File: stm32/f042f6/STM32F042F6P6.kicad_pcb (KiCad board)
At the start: 2 copper layers, 22.9 x 32.1 mm, 29 parts, among them J1 USB_C_REC_16PIN, J2 STLINK, J3 L, J4 R, SW1 BOOT0, U1 XC6220B331MR, U2 STM32F042F6Px, Y1 8 MHz

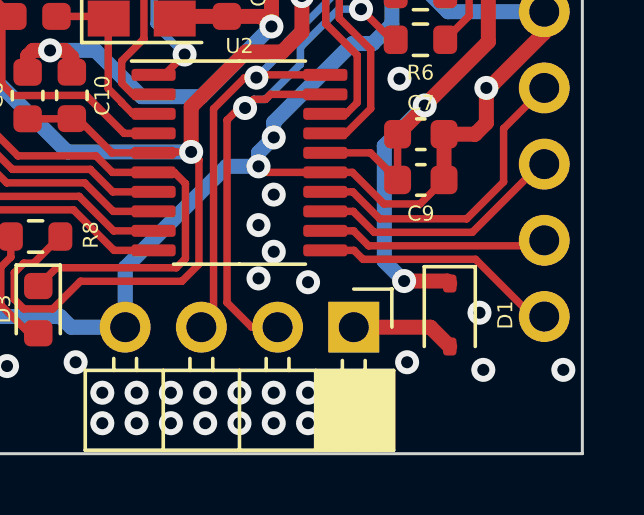
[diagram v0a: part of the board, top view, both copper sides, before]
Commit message: WIP: F070F6P6, Fix: Diode direction corrected for F042F6P6.
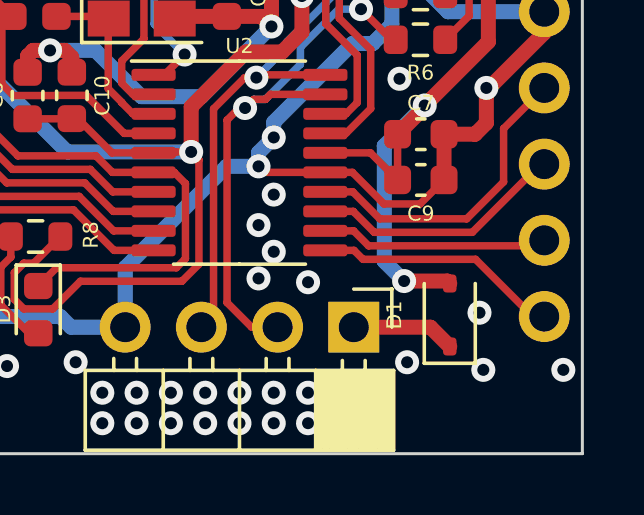
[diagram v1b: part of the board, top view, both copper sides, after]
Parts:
- C3, C4: value 8pF -> 32pF
- turned D1 to 90 degrees
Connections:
- D1 pad 1: +3.3V -> Net-(D1-K)
- D1 pad 2: Net-(D1-A) -> +3.3V
- J2 pad 1: Net-(D1-A) -> Net-(D1-K)
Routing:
- net Net-(D1-K): track 0.00 -> 3.47 mm
- net Net-(D1-A): track 3.47 -> 0.00 mm
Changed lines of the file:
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@@
   (net 6 "+3.3V")
   (net 7 "NRST")
-  (net 8 "Net-(D1-A)")
+  (net 8 "Net-(D1-K)")
   (net 9 "Net-(D2-A)")
   (net 10 "Net-(J1-CC1)")
@@
       (stroke (width 0.1) (type solid)) (layer "F.Fab"))
     (pad "1" thru_hole rect (at 0 0 270) (size 1.7 1.7) (drill 1) (layers "*.Cu" "*.Mask")
-      (net 8 "Net-(D1-A)") (pinfunction "Pin_1") (pintype "passive"))
+      (net 8 "Net-(D1-K)") (pinfunction "Pin_1") (pintype "passive"))
     (pad "2" thru_hole oval (at 0 2.54 270) (size 1.7 1.7) (drill 1) (layers "*.Cu" "*.Mask")
       (net 16 "SWDIO") (pinfunction "Pin_2") (pintype "passive"))
@@
         (effects (font (size 0.5 0.5) (thickness 0.125)))
     )
-    (fp_text value "8pF" (at 0 1.43 90) (layer "F.Fab")
+    (fp_text value "32pF" (at 0 1.43 90) (layer "F.Fab")
         (effects (font (size 1 1) (thickness 0.15)))
     )
@@
   )
   (footprint "Diode_SMD:D_SOD-323" (layer "F.Cu")
-    (at 97.1804 104.0892 -90)
+    (at 97.1804 104.0892 90)
     (descr "SOD-323")
     (tags "SOD-323")
@@
     (fp_line (start 0.9 0.7) (end -0.9 0.7)
       (stroke (width 0.1) (type solid)) (layer "F.Fab"))
-    (pad "1" smd roundrect (at -1.05 0 270) (size 0.6 0.45) (layers "F.Cu" "F.Paste" "F.Mask") (roundrect_rratio 0.25)
-      (net 6 "+3.3V") (pinfunction "K") (pintype "passive"))
-    (pad "2" smd roundrect (at 1.05 0 270) (size 0.6 0.45) (layers "F.Cu" "F.Paste" "F.Mask") (roundrect_rratio 0.25)
-      (net 8 "Net-(D1-A)") (pinfunction "A") (pintype "passive"))
+    (pad "1" smd roundrect (at -1.05 0 90) (size 0.6 0.45) (layers "F.Cu" "F.Paste" "F.Mask") (roundrect_rratio 0.25)
+      (net 8 "Net-(D1-K)") (pinfunction "K") (pintype "passive"))
+    (pad "2" smd roundrect (at 1.05 0 90) (size 0.6 0.45) (layers "F.Cu" "F.Paste" "F.Mask") (roundrect_rratio 0.25)
+      (net 6 "+3.3V") (pinfunction "A") (pintype "passive"))
     (model "${KICAD6_3DMODEL_DIR}/Diode_SMD.3dshapes/D_SOD-323.wrl"
       (offset (xyz 0 0 0))
@@
         (effects (font (size 0.5 0.5) (thickness 0.125)))
     )
-    (fp_text value "8pF" (at 0 1.43 90) (layer "F.Fab")
-        (effects (font (size 1 1) (thickness 0.15)))
-    )
+    (fp_text value "32pF" (at 0 1.43 90) (layer "F.Fab")
+        (effects (font (size 1 1) (thickness 0.15)))
+    )

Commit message: Fix: Diode direction corrected.
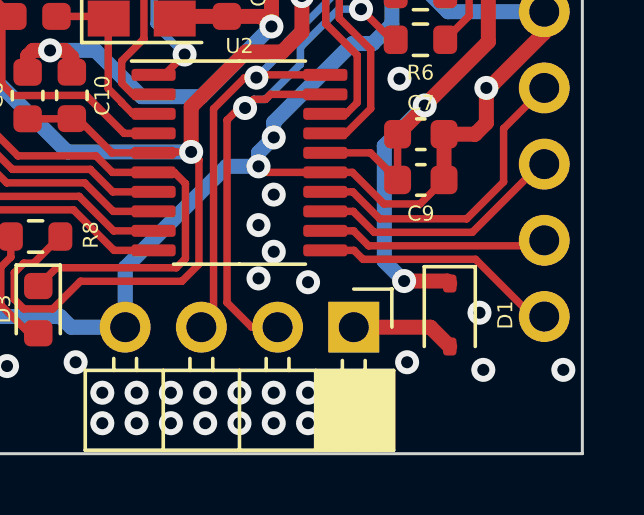
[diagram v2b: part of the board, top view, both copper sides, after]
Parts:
- turned D1 to -90 degrees
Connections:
- D1 pad 1: Net-(D1-K) -> +3.3V
- D1 pad 2: +3.3V -> Net-(D1-A)
- J2 pad 1: Net-(D1-K) -> Net-(D1-A)
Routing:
- net Net-(D1-K): track 3.47 -> 0.00 mm
- net Net-(D1-A): track 0.00 -> 3.47 mm
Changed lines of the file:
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@@
   (net 6 "+3.3V")
   (net 7 "NRST")
-  (net 8 "Net-(D1-K)")
+  (net 8 "Net-(D1-A)")
   (net 9 "Net-(D2-A)")
   (net 10 "Net-(J1-CC1)")
@@
       (stroke (width 0.1) (type solid)) (layer "F.Fab"))
     (pad "1" thru_hole rect (at 0 0 270) (size 1.7 1.7) (drill 1) (layers "*.Cu" "*.Mask")
-      (net 8 "Net-(D1-K)") (pinfunction "Pin_1") (pintype "passive"))
+      (net 8 "Net-(D1-A)") (pinfunction "Pin_1") (pintype "passive"))
     (pad "2" thru_hole oval (at 0 2.54 270) (size 1.7 1.7) (drill 1) (layers "*.Cu" "*.Mask")
       (net 16 "SWDIO") (pinfunction "Pin_2") (pintype "passive"))
@@
   )
   (footprint "Diode_SMD:D_SOD-323" (layer "F.Cu")
-    (at 97.1804 104.0892 90)
+    (at 97.1804 104.0892 -90)
     (descr "SOD-323")
     (tags "SOD-323")
@@
     (fp_line (start 0.9 0.7) (end -0.9 0.7)
       (stroke (width 0.1) (type solid)) (layer "F.Fab"))
-    (pad "1" smd roundrect (at -1.05 0 90) (size 0.6 0.45) (layers "F.Cu" "F.Paste" "F.Mask") (roundrect_rratio 0.25)
-      (net 8 "Net-(D1-K)") (pinfunction "K") (pintype "passive"))
-    (pad "2" smd roundrect (at 1.05 0 90) (size 0.6 0.45) (layers "F.Cu" "F.Paste" "F.Mask") (roundrect_rratio 0.25)
-      (net 6 "+3.3V") (pinfunction "A") (pintype "passive"))
+    (pad "1" smd roundrect (at -1.05 0 270) (size 0.6 0.45) (layers "F.Cu" "F.Paste" "F.Mask") (roundrect_rratio 0.25)
+      (net 6 "+3.3V") (pinfunction "K") (pintype "passive"))
+    (pad "2" smd roundrect (at 1.05 0 270) (size 0.6 0.45) (layers "F.Cu" "F.Paste" "F.Mask") (roundrect_rratio 0.25)
+      (net 8 "Net-(D1-A)") (pinfunction "A") (pintype "passive"))
     (model "${KICAD6_3DMODEL_DIR}/Diode_SMD.3dshapes/D_SOD-323.wrl"
       (offset (xyz 0 0 0))

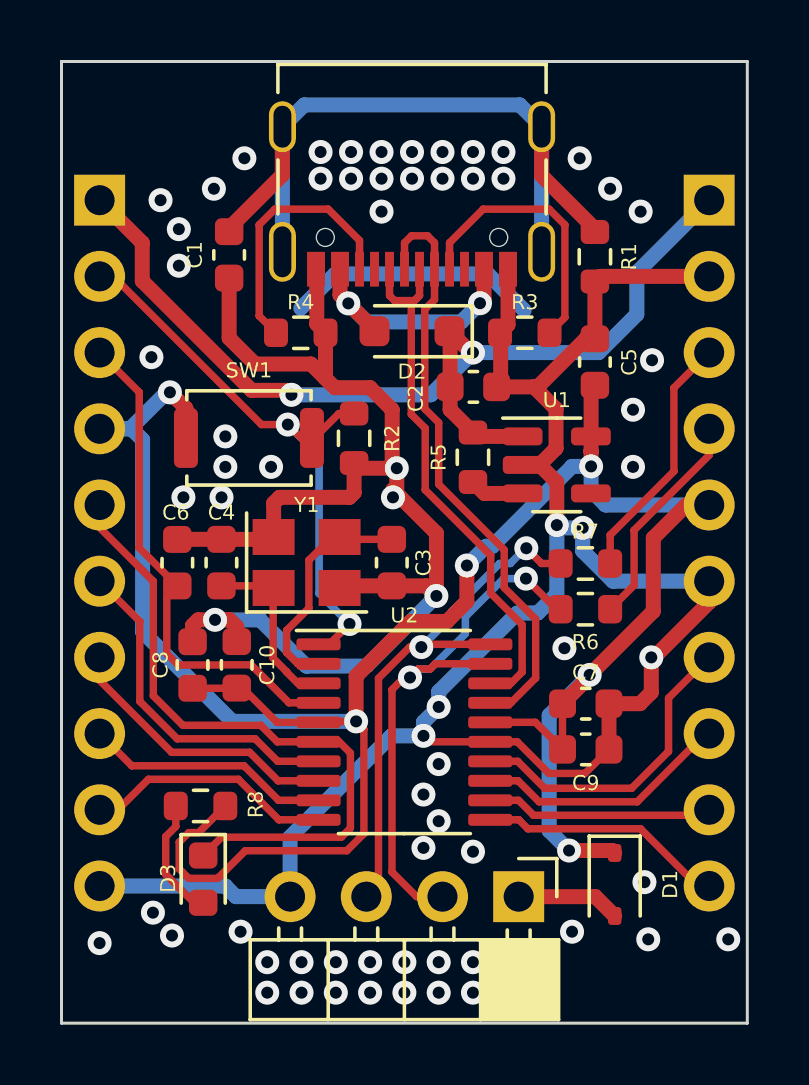
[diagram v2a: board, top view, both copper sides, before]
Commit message: F042: HSE crystal removal because it didn't be needed.
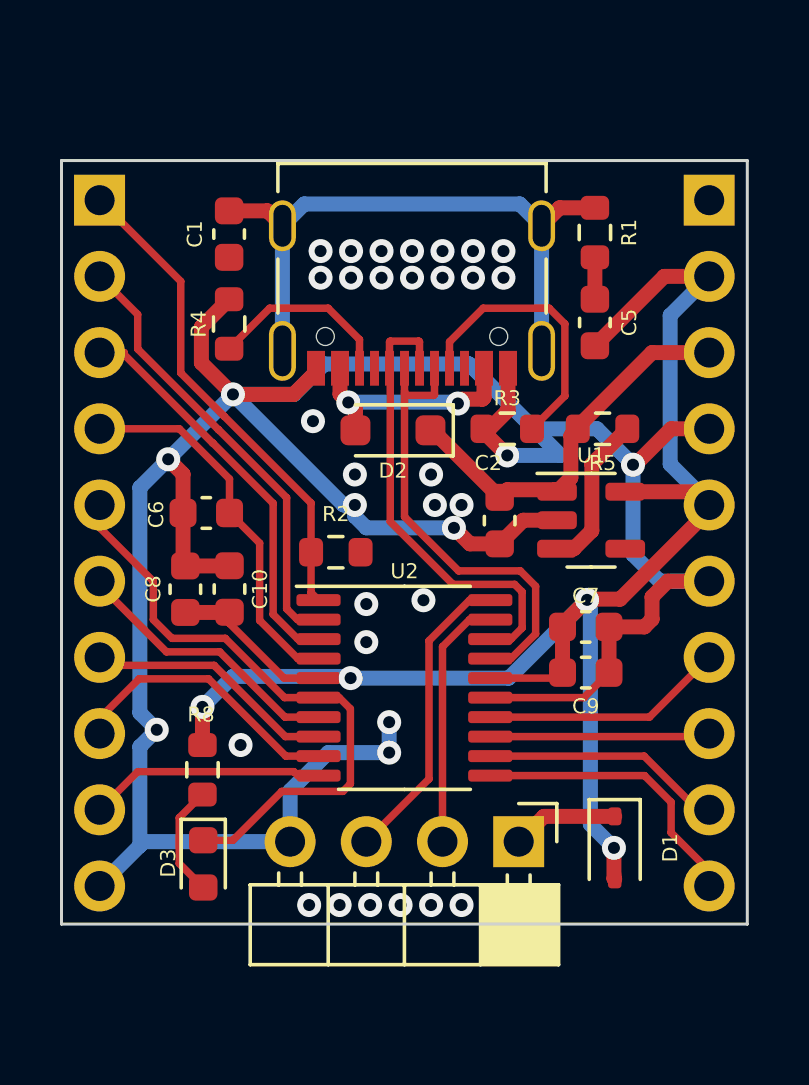
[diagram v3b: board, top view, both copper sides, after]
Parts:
- removed C3, C4: 32pF, Capacitor_SMD:C_0603_1608Metric
- removed R6, R7: 0, Resistor_SMD:R_0603_1608Metric
- removed SW1: BOOT0, Button_Switch_SMD:SW_Push_SPST_NO_Alps_SKRK
- removed Y1: 8 MHz, Crystal:Crystal_SMD_3225-4Pin_3.2x2.5mm
- moved C2 4.54 mm to (93.3, 92.0), turned to 90 degrees
- moved R5 4.42 mm to (96.8, 88.9), turned to 180 degrees
- moved R2 3.85 mm to (87.9, 93.0), turned to 180 degrees
- moved D2 3.36 mm to (89.8, 89.0)
- moved J1 3.30 mm to (90.4, 84.4)
- moved R3 3.25 mm to (93.6, 88.9)
- moved C7 2.56 mm to (96.2, 95.5)
- moved C9 2.56 mm to (96.2, 97.0)
- moved C10 2.54 mm to (82.9, 94.2)
- moved C8 2.54 mm to (84.3, 94.2)
- moved R4 2.41 mm to (84.3, 85.4), turned to 90 degrees
- moved U1 2.17 mm to (96.4, 91.9)
- moved C6 1.92 mm to (83.6, 91.7), turned to 180 degrees
- moved J2 1.83 mm to (94.0, 102.7)
- moved U2 1.47 mm to (90.2, 97.5)
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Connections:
- D1 pad 1: +3.3V -> Net-(D1-K)
- D1 pad 2: Net-(D1-A) -> +3.3V
- J2 pad 1: Net-(D1-A) -> Net-(D1-K)
- J3 pad 1: +5V -> PB8/BOOT0
- J3 pad 2: PB8/BOOT0 -> PF0/HSE_IN
- J3 pad 3: NRST -> PF1/HSE_OUT
- J3 pad 4: +3.3V -> NRST
- J4 pad 2: GND -> +3.3V
- J4 pad 3: PA14 -> +5V
- J4 pad 4: PA13 -> GND
- U2 pad 2: HSE_IN -> PF0/HSE_IN
- U2 pad 3: HSE_OUT -> PF1/HSE_OUT
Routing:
- net +3.3V: track 83.0 -> 59.1 mm, vias 6 -> 4
- net +5V: track 33.7 -> 13.1 mm, vias 2 -> 0
- net GND: track 117.0 -> 101.8 mm, vias 73 -> 39
- net PF0/HSE_IN: track 0.00 -> 14.9 mm
- net PF1/HSE_OUT: track 0.00 -> 13.5 mm
- net SWDIO: track 18.9 -> 8.46 mm, vias 2 -> 0
- net PA14: track 8.40 -> 0.00 mm
- net HSE_IN: track 7.66 -> 0.00 mm
- net PA13: track 7.38 -> 0.00 mm
- net SWCLK: track 18.0 -> 10.6 mm, vias 2 -> 0
- net HSE_OUT: track 5.98 -> 0.00 mm
- net Net-(J1-SHIELD): track 26.1 -> 21.6 mm
- net NRST: track 17.0 -> 12.6 mm
- net USB_DM: track 20.1 -> 15.8 mm
- net Net-(D1-K): track 0.00 -> 3.55 mm
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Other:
- board size 22.9 x 32.1 mm -> 22.9 x 25.5 mm
- board text added: "5V 3V3 5V GND 3V3 GND B1 A7 A6 A5"
- board text added: "B8 F0 F1 NRST A0 A1 A2 A3 A4 GND"
- board text removed: "5V B8 NRST 3V3 A0 A1 A2 A3 A4 GND"
- board text removed: "5V GND A14 A13 3V3 GND B1 A7 A6 A5"
